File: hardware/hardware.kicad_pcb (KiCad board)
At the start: 2 copper layers, 1 part, among them U1 CH32V003F4P6

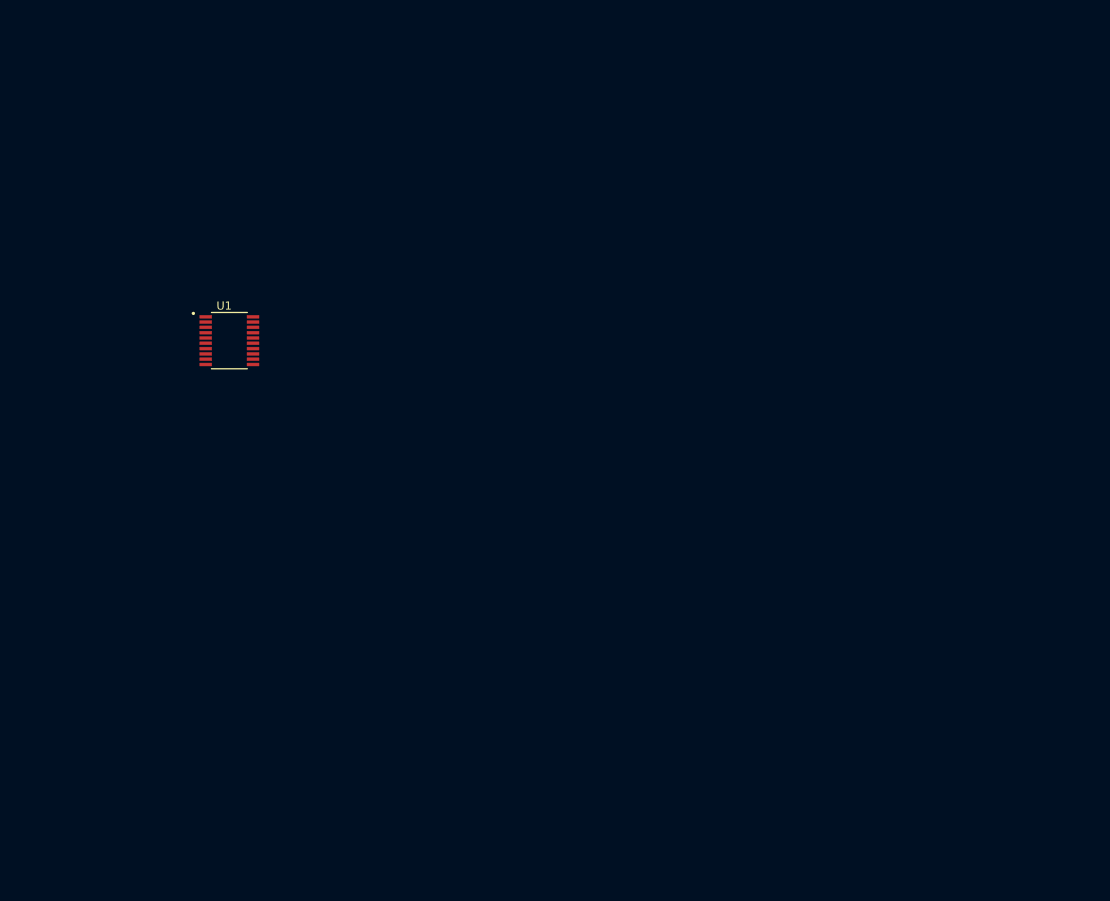
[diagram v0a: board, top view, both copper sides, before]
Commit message: add ch32v003 on pcb
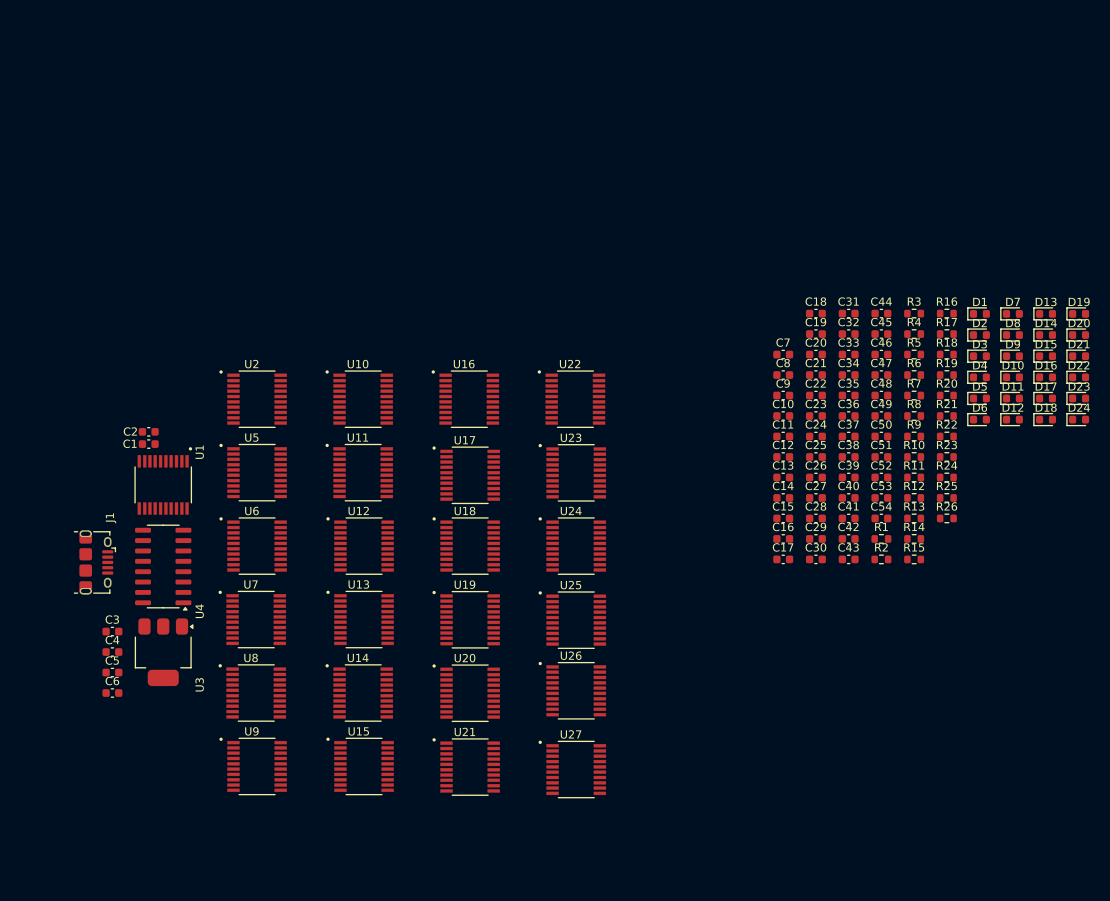
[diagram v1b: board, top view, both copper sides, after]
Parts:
- added C1: C_Small, Capacitor_SMD:C_0603_1608Metric, F.Cu at (49.7, 54.5)
- added C10: C_Small, Capacitor_SMD:C_0603_1608Metric, F.Cu at (127.5, 51.1)
- added C11: C_Small, Capacitor_SMD:C_0603_1608Metric, F.Cu at (127.5, 53.6)
- added C12: C_Small, Capacitor_SMD:C_0603_1608Metric, F.Cu at (127.5, 56.1)
- added C13: C_Small, Capacitor_SMD:C_0603_1608Metric, F.Cu at (127.5, 58.6)
- added C14: C_Small, Capacitor_SMD:C_0603_1608Metric, F.Cu at (127.5, 61.1)
- added C15: C_Small, Capacitor_SMD:C_0603_1608Metric, F.Cu at (127.5, 63.6)
- added C16: C_Small, Capacitor_SMD:C_0603_1608Metric, F.Cu at (127.5, 66.1)
- added C17: C_Small, Capacitor_SMD:C_0603_1608Metric, F.Cu at (127.5, 68.6)
- added C18: C_Small, Capacitor_SMD:C_0603_1608Metric, F.Cu at (131.5, 38.5)
- added C19: C_Small, Capacitor_SMD:C_0603_1608Metric, F.Cu at (131.5, 41.0)
- added C2: C_Small, Capacitor_SMD:C_0603_1608Metric, F.Cu at (49.7, 53.0)
- added C20: C_Small, Capacitor_SMD:C_0603_1608Metric, F.Cu at (131.5, 43.5)
- added C21: C_Small, Capacitor_SMD:C_0603_1608Metric, F.Cu at (131.5, 46.0)
- added C22: C_Small, Capacitor_SMD:C_0603_1608Metric, F.Cu at (131.5, 48.5)
- added C23: C_Small, Capacitor_SMD:C_0603_1608Metric, F.Cu at (131.5, 51.1)
- added C24: C_Small, Capacitor_SMD:C_0603_1608Metric, F.Cu at (131.5, 53.6)
- added C25: C_Small, Capacitor_SMD:C_0603_1608Metric, F.Cu at (131.5, 56.1)
- added C26: C_Small, Capacitor_SMD:C_0603_1608Metric, F.Cu at (131.5, 58.6)
- added C27: C_Small, Capacitor_SMD:C_0603_1608Metric, F.Cu at (131.5, 61.1)
- added C28: C_Small, Capacitor_SMD:C_0603_1608Metric, F.Cu at (131.5, 63.6)
- added C29: C_Small, Capacitor_SMD:C_0603_1608Metric, F.Cu at (131.5, 66.1)
- added C3: C, Capacitor_SMD:C_0603_1608Metric, F.Cu at (45.3, 77.5)
- added C30: C_Small, Capacitor_SMD:C_0603_1608Metric, F.Cu at (131.5, 68.6)
- added C31: C_Small, Capacitor_SMD:C_0603_1608Metric, F.Cu at (135.5, 38.5)
- added C32: C_Small, Capacitor_SMD:C_0603_1608Metric, F.Cu at (135.5, 41.0)
- added C33: C_Small, Capacitor_SMD:C_0603_1608Metric, F.Cu at (135.5, 43.5)
- added C34: C_Small, Capacitor_SMD:C_0603_1608Metric, F.Cu at (135.5, 46.0)
- added C35: C_Small, Capacitor_SMD:C_0603_1608Metric, F.Cu at (135.5, 48.5)
- added C36: C_Small, Capacitor_SMD:C_0603_1608Metric, F.Cu at (135.5, 51.1)
- added C37: C_Small, Capacitor_SMD:C_0603_1608Metric, F.Cu at (135.5, 53.6)
- added C38: C_Small, Capacitor_SMD:C_0603_1608Metric, F.Cu at (135.5, 56.1)
- added C39: C_Small, Capacitor_SMD:C_0603_1608Metric, F.Cu at (135.5, 58.6)
- added C4: C, Capacitor_SMD:C_0603_1608Metric, F.Cu at (45.3, 80.0)
- added C40: C_Small, Capacitor_SMD:C_0603_1608Metric, F.Cu at (135.5, 61.1)
- added C41: C_Small, Capacitor_SMD:C_0603_1608Metric, F.Cu at (135.5, 63.6)
- added C42: C_Small, Capacitor_SMD:C_0603_1608Metric, F.Cu at (135.5, 66.1)
- added C43: C_Small, Capacitor_SMD:C_0603_1608Metric, F.Cu at (135.5, 68.6)
- added C44: C_Small, Capacitor_SMD:C_0603_1608Metric, F.Cu at (139.5, 38.5)
- added C45: C_Small, Capacitor_SMD:C_0603_1608Metric, F.Cu at (139.5, 41.0)
- added C46: C_Small, Capacitor_SMD:C_0603_1608Metric, F.Cu at (139.5, 43.5)
- added C47: C_Small, Capacitor_SMD:C_0603_1608Metric, F.Cu at (139.5, 46.0)
- added C48: C_Small, Capacitor_SMD:C_0603_1608Metric, F.Cu at (139.5, 48.5)
- added C49: C_Small, Capacitor_SMD:C_0603_1608Metric, F.Cu at (139.5, 51.1)
- added C5: C, Capacitor_SMD:C_0603_1608Metric, F.Cu at (45.3, 82.5)
- added C50: C_Small, Capacitor_SMD:C_0603_1608Metric, F.Cu at (139.5, 53.6)
- added C51: C_Small, Capacitor_SMD:C_0603_1608Metric, F.Cu at (139.5, 56.1)
- added C52: C_Small, Capacitor_SMD:C_0603_1608Metric, F.Cu at (139.5, 58.6)
- added C53: C_Small, Capacitor_SMD:C_0603_1608Metric, F.Cu at (139.5, 61.1)
- added C54: C_Small, Capacitor_SMD:C_0603_1608Metric, F.Cu at (139.5, 63.6)
- added C6: C, Capacitor_SMD:C_0603_1608Metric, F.Cu at (45.3, 85.0)
- added C7: C_Small, Capacitor_SMD:C_0603_1608Metric, F.Cu at (127.5, 43.5)
- added C8: C_Small, Capacitor_SMD:C_0603_1608Metric, F.Cu at (127.5, 46.0)
- added C9: C_Small, Capacitor_SMD:C_0603_1608Metric, F.Cu at (127.5, 48.5)
- added D1: LED, LED_SMD:LED_0603_1608Metric, F.Cu at (151.6, 38.5)
- added D10: LED, LED_SMD:LED_0603_1608Metric, F.Cu at (155.6, 46.3)
- added D11: LED, LED_SMD:LED_0603_1608Metric, F.Cu at (155.6, 48.9)
- added D12: LED, LED_SMD:LED_0603_1608Metric, F.Cu at (155.6, 51.5)
- added D13: LED, LED_SMD:LED_0603_1608Metric, F.Cu at (159.7, 38.5)
- added D14: LED, LED_SMD:LED_0603_1608Metric, F.Cu at (159.7, 41.1)
- added D15: LED, LED_SMD:LED_0603_1608Metric, F.Cu at (159.7, 43.7)
- added D16: LED, LED_SMD:LED_0603_1608Metric, F.Cu at (159.7, 46.3)
- added D17: LED, LED_SMD:LED_0603_1608Metric, F.Cu at (159.7, 48.9)
- added D18: LED, LED_SMD:LED_0603_1608Metric, F.Cu at (159.7, 51.5)
- added D19: LED, LED_SMD:LED_0603_1608Metric, F.Cu at (163.7, 38.5)
- added D2: LED, LED_SMD:LED_0603_1608Metric, F.Cu at (151.6, 41.1)
- added D20: LED, LED_SMD:LED_0603_1608Metric, F.Cu at (163.7, 41.1)
- added D21: LED, LED_SMD:LED_0603_1608Metric, F.Cu at (163.7, 43.7)
- added D22: LED, LED_SMD:LED_0603_1608Metric, F.Cu at (163.7, 46.3)
- added D23: LED, LED_SMD:LED_0603_1608Metric, F.Cu at (163.7, 48.9)
- added D24: LED, LED_SMD:LED_0603_1608Metric, F.Cu at (163.7, 51.5)
- added D3: LED, LED_SMD:LED_0603_1608Metric, F.Cu at (151.6, 43.7)
- added D4: LED, LED_SMD:LED_0603_1608Metric, F.Cu at (151.6, 46.3)
- added D5: LED, LED_SMD:LED_0603_1608Metric, F.Cu at (151.6, 48.9)
- added D6: LED, LED_SMD:LED_0603_1608Metric, F.Cu at (151.6, 51.5)
- added D7: LED, LED_SMD:LED_0603_1608Metric, F.Cu at (155.6, 38.5)
- added D8: LED, LED_SMD:LED_0603_1608Metric, F.Cu at (155.6, 41.1)
- added D9: LED, LED_SMD:LED_0603_1608Metric, F.Cu at (155.6, 43.7)
- added J1: USB_B_Micro, Connector_USB:USB_Micro-B_Amphenol_10118194_Horizontal, F.Cu at (43.3, 69.0)
- added R1: R_Small, Resistor_SMD:R_0603_1608Metric, F.Cu at (139.5, 66.1)
- added R10: R_Small, Resistor_SMD:R_0603_1608Metric, F.Cu at (143.5, 56.1)
- added R11: R_Small, Resistor_SMD:R_0603_1608Metric, F.Cu at (143.5, 58.6)
- added R12: R_Small, Resistor_SMD:R_0603_1608Metric, F.Cu at (143.5, 61.1)
- added R13: R_Small, Resistor_SMD:R_0603_1608Metric, F.Cu at (143.5, 63.6)
- added R14: R_Small, Resistor_SMD:R_0603_1608Metric, F.Cu at (143.5, 66.1)
- added R15: R_Small, Resistor_SMD:R_0603_1608Metric, F.Cu at (143.5, 68.6)
- added R16: R_Small, Resistor_SMD:R_0603_1608Metric, F.Cu at (147.5, 38.5)
- added R17: R_Small, Resistor_SMD:R_0603_1608Metric, F.Cu at (147.5, 41.0)
- added R18: R_Small, Resistor_SMD:R_0603_1608Metric, F.Cu at (147.5, 43.5)
- added R19: R_Small, Resistor_SMD:R_0603_1608Metric, F.Cu at (147.5, 46.0)
- added R2: R_Small, Resistor_SMD:R_0603_1608Metric, F.Cu at (139.5, 68.6)
- added R20: R_Small, Resistor_SMD:R_0603_1608Metric, F.Cu at (147.5, 48.5)
- added R21: R_Small, Resistor_SMD:R_0603_1608Metric, F.Cu at (147.5, 51.1)
- added R22: R_Small, Resistor_SMD:R_0603_1608Metric, F.Cu at (147.5, 53.6)
- added R23: R_Small, Resistor_SMD:R_0603_1608Metric, F.Cu at (147.5, 56.1)
- added R24: R_Small, Resistor_SMD:R_0603_1608Metric, F.Cu at (147.5, 58.6)
- added R25: R_Small, Resistor_SMD:R_0603_1608Metric, F.Cu at (147.5, 61.1)
- added R26: R_Small, Resistor_SMD:R_0603_1608Metric, F.Cu at (147.5, 63.6)
- added R3: R_Small, Resistor_SMD:R_0603_1608Metric, F.Cu at (143.5, 38.5)
- added R4: R_Small, Resistor_SMD:R_0603_1608Metric, F.Cu at (143.5, 41.0)
- added R5: R_Small, Resistor_SMD:R_0603_1608Metric, F.Cu at (143.5, 43.5)
- added R6: R_Small, Resistor_SMD:R_0603_1608Metric, F.Cu at (143.5, 46.0)
- added R7: R_Small, Resistor_SMD:R_0603_1608Metric, F.Cu at (143.5, 48.5)
- added R8: R_Small, Resistor_SMD:R_0603_1608Metric, F.Cu at (143.5, 51.1)
- added R9: R_Small, Resistor_SMD:R_0603_1608Metric, F.Cu at (143.5, 53.6)
- added U10: CH32V003F4P6, CH32V003F4P6:SOP65P640X121-20N, F.Cu at (76.0, 49.0)
- added U11: CH32V003F4P6, CH32V003F4P6:SOP65P640X121-20N, F.Cu at (76.0, 58.0)
- added U12: CH32V003F4P6, CH32V003F4P6:SOP65P640X121-20N, F.Cu at (76.1, 67.0)
- added U13: CH32V003F4P6, CH32V003F4P6:SOP65P640X121-20N, F.Cu at (76.1, 76.0)
- added U14: CH32V003F4P6, CH32V003F4P6:SOP65P640X121-20N, F.Cu at (76.0, 85.0)
- added U15: CH32V003F4P6, CH32V003F4P6:SOP65P640X121-20N, F.Cu at (76.1, 94.0)
- added U16: CH32V003F4P6, CH32V003F4P6:SOP65P640X121-20N, F.Cu at (89.0, 49.0)
- added U17: CH32V003F4P6, CH32V003F4P6:SOP65P640X121-20N, F.Cu at (89.1, 58.3)
- added U18: CH32V003F4P6, CH32V003F4P6:SOP65P640X121-20N, F.Cu at (89.1, 67.0)
- added U19: CH32V003F4P6, CH32V003F4P6:SOP65P640X121-20N, F.Cu at (89.1, 76.0)
- added U2: CH32V003F4P6, CH32V003F4P6:SOP65P640X121-20N, F.Cu at (63.0, 49.0)
- added U20: CH32V003F4P6, CH32V003F4P6:SOP65P640X121-20N, F.Cu at (89.1, 85.0)
- added U21: CH32V003F4P6, CH32V003F4P6:SOP65P640X121-20N, F.Cu at (89.1, 94.1)
- added U22: CH32V003F4P6, CH32V003F4P6:SOP65P640X121-20N, F.Cu at (102.0, 49.0)
- added U23: CH32V003F4P6, CH32V003F4P6:SOP65P640X121-20N, F.Cu at (102.1, 58.0)
- added U24: CH32V003F4P6, CH32V003F4P6:SOP65P640X121-20N, F.Cu at (102.1, 67.0)
- added U25: CH32V003F4P6, CH32V003F4P6:SOP65P640X121-20N, F.Cu at (102.1, 76.1)
- added U26: CH32V003F4P6, CH32V003F4P6:SOP65P640X121-20N, F.Cu at (102.1, 84.7)
- added U27: CH32V003F4P6, CH32V003F4P6:SOP65P640X121-20N, F.Cu at (102.1, 94.4)
- added U3: AMS1117-3.3, Package_TO_SOT_SMD:SOT-223-3_TabPin2, F.Cu at (51.5, 80.0)
- added U4: CH340C, Package_SO:SOIC-16_3.9x9.9mm_P1.27mm, F.Cu at (51.5, 69.5)
- added U5: CH32V003F4P6, CH32V003F4P6:SOP65P640X121-20N, F.Cu at (63.0, 58.0)
- added U6: CH32V003F4P6, CH32V003F4P6:SOP65P640X121-20N, F.Cu at (63.0, 67.0)
- added U7: CH32V003F4P6, CH32V003F4P6:SOP65P640X121-20N, F.Cu at (62.9, 76.0)
- added U8: CH32V003F4P6, CH32V003F4P6:SOP65P640X121-20N, F.Cu at (62.9, 85.0)
- added U9: CH32V003F4P6, CH32V003F4P6:SOP65P640X121-20N, F.Cu at (63.0, 94.0)
- moved U1 19.4 mm to (51.5, 59.5), turned to -90 degrees
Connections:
- U1 pad 11: unconnected-(U1-PC1/SDA/NSS-Pad11) -> SDA
- U1 pad 12: unconnected-(U1-PC2/SCL/URTS/T1BKIN-Pad12) -> SCL
- U1 pad 18: unconnected-(U1-PD1/SWIO/T1CH3N/AETR2-Pad18) -> DIO0
- U1 pad 2: unconnected-(U1-PD5/UTX/A5-Pad2) -> RX-PROG
- U1 pad 3: unconnected-(U1-PD6/URX/A6-Pad3) -> TX-PROG
- U1 pad 7: unconnected-(U1-VSS-Pad7) -> GND
- U1 pad 9: unconnected-(U1-VDD-Pad9) -> +3V3

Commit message: position capacitor + resistor + led with each ch32
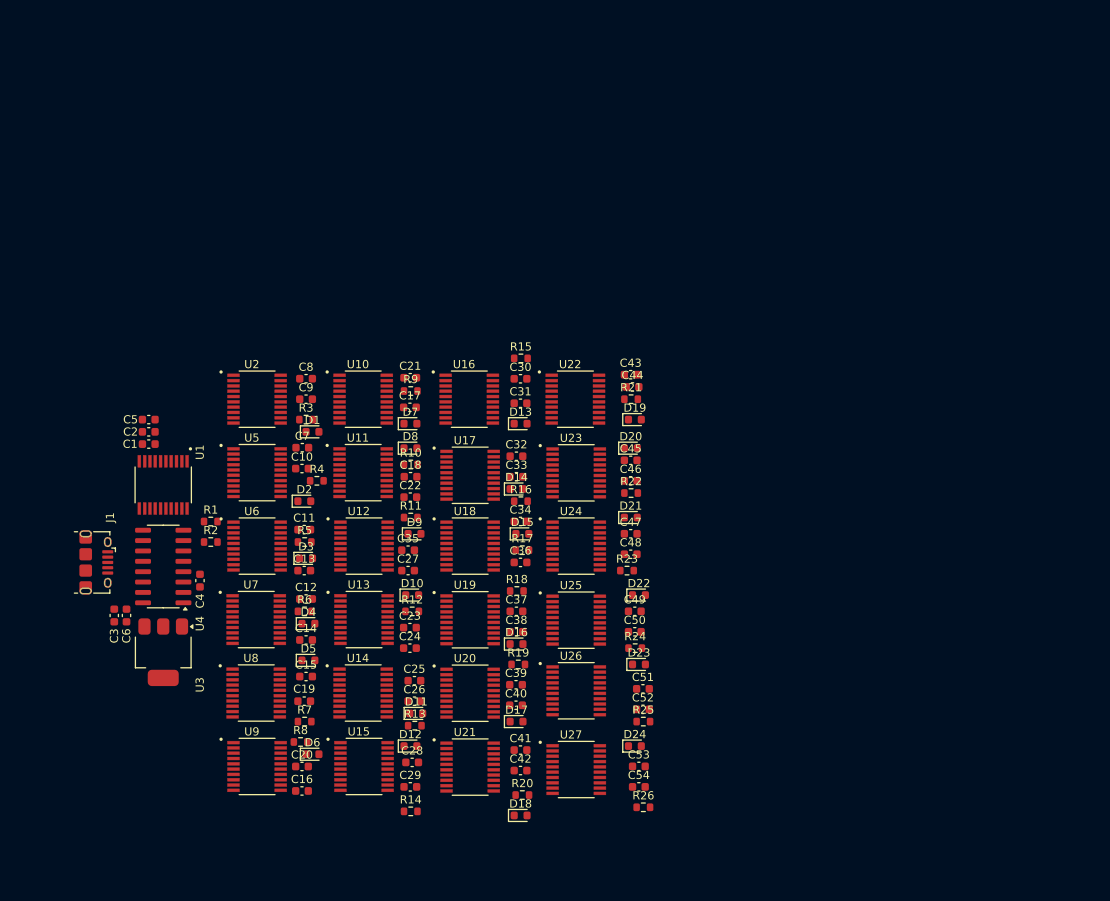
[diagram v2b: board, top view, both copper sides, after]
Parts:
- moved D6 91.5 mm to (69.8, 92.5)
- moved D5 88.3 mm to (69.3, 81.0)
- moved D4 87.6 mm to (69.3, 76.5)
- moved D3 86.2 mm to (69.0, 68.5)
- moved D2 85.2 mm to (68.8, 61.5)
- moved R8 85.1 mm to (68.3, 91.0)
- moved R7 84.7 mm to (68.8, 88.5)
- moved D12 84.0 mm to (81.8, 91.5)
- moved D1 83.0 mm to (69.8, 53.0)
- moved D11 82.7 mm to (82.5, 87.5)
- moved R1 82.2 mm to (57.3, 64.0)
- moved R2 82.2 mm to (57.3, 66.5)
- moved C20 80.7 mm to (68.5, 94.0)
- moved D18 80.6 mm to (95.3, 100.0)
- moved R6 80.1 mm to (68.8, 75.0)
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
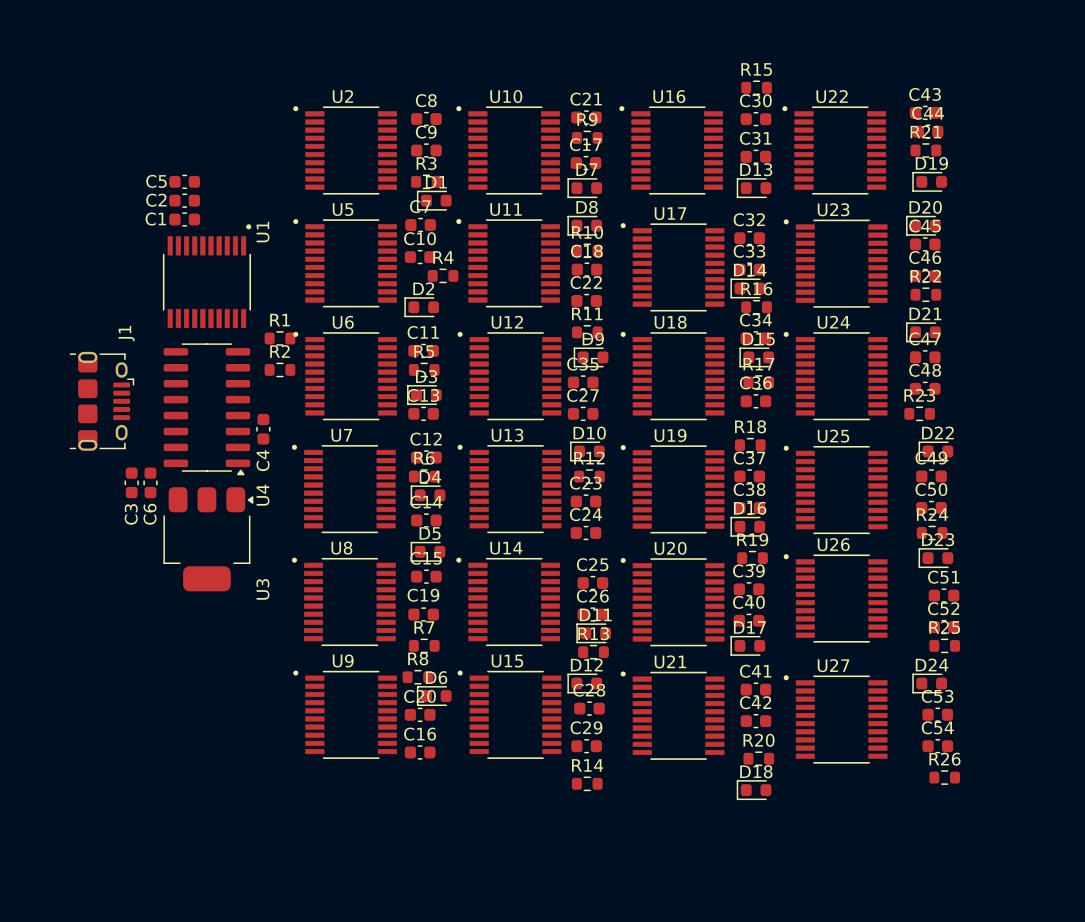
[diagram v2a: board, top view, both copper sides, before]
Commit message: add wiring ch32v006
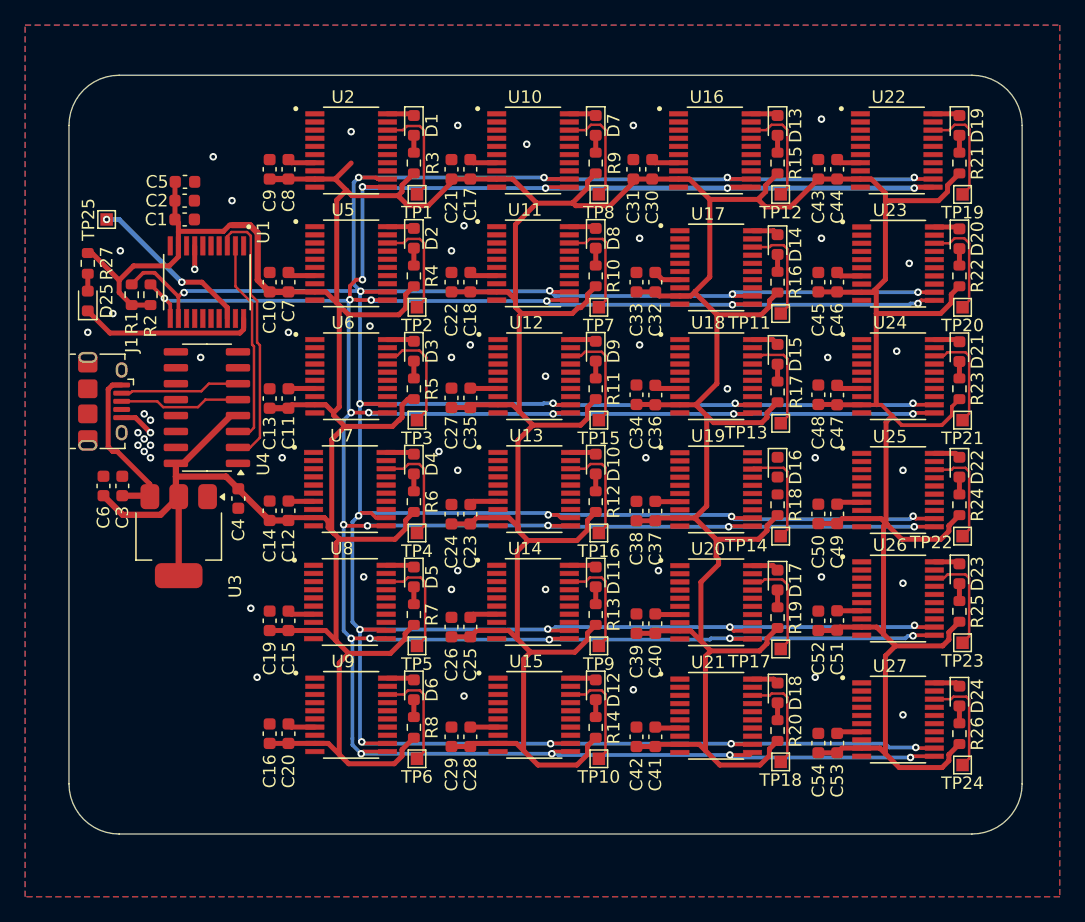
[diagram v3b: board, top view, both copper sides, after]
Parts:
- added D25: LED, LED_SMD:LED_0603_1608Metric, F.Cu at (42.0, 61.0)
- added R27: R_Small, Resistor_SMD:R_0603_1608Metric, F.Cu at (42.0, 58.0)
- added TP1: TestPoint, TestPoint:TestPoint_Pad_1.0x1.0mm, F.Cu at (68.2, 52.5)
- added TP10: TestPoint, TestPoint:TestPoint_Pad_1.0x1.0mm, F.Cu at (82.8, 97.5)
- added TP11: TestPoint, TestPoint:TestPoint_Pad_1.0x1.0mm, F.Cu at (97.2, 62.0)
- added TP12: TestPoint, TestPoint:TestPoint_Pad_1.0x1.0mm, F.Cu at (97.2, 52.5)
- added TP13: TestPoint, TestPoint:TestPoint_Pad_1.0x1.0mm, F.Cu at (97.2, 70.8)
- added TP14: TestPoint, TestPoint:TestPoint_Pad_1.0x1.0mm, F.Cu at (97.2, 79.8)
- added TP15: TestPoint, TestPoint:TestPoint_Pad_1.0x1.0mm, F.Cu at (82.8, 70.5)
- added TP16: TestPoint, TestPoint:TestPoint_Pad_1.0x1.0mm, F.Cu at (82.8, 79.5)
- added TP17: TestPoint, TestPoint:TestPoint_Pad_1.0x1.0mm, F.Cu at (97.2, 88.8)
- added TP18: TestPoint, TestPoint:TestPoint_Pad_1.0x1.0mm, F.Cu at (97.2, 97.8)
- added TP19: TestPoint, TestPoint:TestPoint_Pad_1.0x1.0mm, F.Cu at (111.8, 52.5)
- added TP2: TestPoint, TestPoint:TestPoint_Pad_1.0x1.0mm, F.Cu at (68.2, 61.5)
- added TP20: TestPoint, TestPoint:TestPoint_Pad_1.0x1.0mm, F.Cu at (111.8, 61.5)
- added TP21: TestPoint, TestPoint:TestPoint_Pad_1.0x1.0mm, F.Cu at (111.8, 70.5)
- added TP22: TestPoint, TestPoint:TestPoint_Pad_1.0x1.0mm, F.Cu at (111.8, 79.8)
- added TP23: TestPoint, TestPoint:TestPoint_Pad_1.0x1.0mm, F.Cu at (111.8, 88.2)
- added TP24: TestPoint, TestPoint:TestPoint_Pad_1.0x1.0mm, F.Cu at (111.8, 98.0)
- added TP25: TestPoint, TestPoint:TestPoint_Pad_1.0x1.0mm, F.Cu at (43.5, 54.5)
- added TP3: TestPoint, TestPoint:TestPoint_Pad_1.0x1.0mm, F.Cu at (68.2, 70.5)
- added TP4: TestPoint, TestPoint:TestPoint_Pad_1.0x1.0mm, F.Cu at (68.2, 79.5)
- added TP5: TestPoint, TestPoint:TestPoint_Pad_1.0x1.0mm, F.Cu at (68.2, 88.5)
- added TP6: TestPoint, TestPoint:TestPoint_Pad_1.0x1.0mm, F.Cu at (68.2, 97.5)
- added TP7: TestPoint, TestPoint:TestPoint_Pad_1.0x1.0mm, F.Cu at (82.8, 61.5)
- added TP8: TestPoint, TestPoint:TestPoint_Pad_1.0x1.0mm, F.Cu at (82.8, 52.5)
- added TP9: TestPoint, TestPoint:TestPoint_Pad_1.0x1.0mm, F.Cu at (82.8, 88.5)
- moved C9 12.6 mm to (56.5, 50.5), turned to 90 degrees
- moved C14 12.5 mm to (56.5, 77.7), turned to 90 degrees
- moved C13 12.3 mm to (56.5, 68.8), turned to 90 degrees
- moved R1 12.3 mm to (45.5, 60.5), turned to 90 degrees
- moved C19 12.3 mm to (56.5, 86.5), turned to 90 degrees
- moved C10 12.2 mm to (56.5, 59.5), turned to 90 degrees
- moved C16 12.1 mm to (56.5, 95.5), turned to 90 degrees
- moved R2 11.9 mm to (47.0, 60.5), turned to 90 degrees
- moved C12 11.8 mm to (58.0, 77.7), turned to 90 degrees
- moved C8 11.7 mm to (58.0, 50.5), turned to 90 degrees
- moved C15 11.5 mm to (58.0, 86.5), turned to 90 degrees
- moved C21 11.5 mm to (71.0, 50.5), turned to 90 degrees
- moved C7 11.5 mm to (58.0, 59.5), turned to 90 degrees
- moved C11 11.4 mm to (58.0, 68.8), turned to 90 degrees
- moved C26 11.3 mm to (71.0, 87.0), turned to 90 degrees
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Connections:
- U1 pad 18: DIO0 -> Net-(U1-PD1/SWIO/T1CH3N/AETR2)
- U1 pad 20: unconnected-(U1-PD3/A4/T2CH2/AETR/UCTS-Pad20) -> Net-(D25-K)
- U10 pad 18: DIO1 -> Net-(U10-PD1/SWIO/T1CH3N/AETR2)
- U11 pad 18: DIO1 -> Net-(U11-PD1/SWIO/T1CH3N/AETR2)
- U12 pad 18: DIO1 -> Net-(U12-PD1/SWIO/T1CH3N/AETR2)
- U13 pad 18: DIO1 -> Net-(U13-PD1/SWIO/T1CH3N/AETR2)
- U14 pad 18: DIO1 -> Net-(U14-PD1/SWIO/T1CH3N/AETR2)
- U15 pad 18: DIO1 -> Net-(U15-PD1/SWIO/T1CH3N/AETR2)
- U16 pad 18: DIO1 -> Net-(U16-PD1/SWIO/T1CH3N/AETR2)
- U17 pad 18: DIO1 -> Net-(U17-PD1/SWIO/T1CH3N/AETR2)
- U18 pad 18: DIO1 -> Net-(U18-PD1/SWIO/T1CH3N/AETR2)
- U19 pad 18: DIO1 -> Net-(U19-PD1/SWIO/T1CH3N/AETR2)
- U2 pad 18: DIO1 -> Net-(U2-PD1/SWIO/T1CH3N/AETR2)
- U20 pad 18: DIO1 -> Net-(U20-PD1/SWIO/T1CH3N/AETR2)
- U21 pad 18: DIO1 -> Net-(U21-PD1/SWIO/T1CH3N/AETR2)
- U22 pad 18: DIO1 -> Net-(U22-PD1/SWIO/T1CH3N/AETR2)
- U23 pad 18: DIO1 -> Net-(U23-PD1/SWIO/T1CH3N/AETR2)
- U24 pad 18: DIO1 -> Net-(U24-PD1/SWIO/T1CH3N/AETR2)
- U25 pad 18: DIO1 -> Net-(U25-PD1/SWIO/T1CH3N/AETR2)
- U26 pad 18: DIO1 -> Net-(U26-PD1/SWIO/T1CH3N/AETR2)
- U27 pad 18: DIO1 -> Net-(U27-PD1/SWIO/T1CH3N/AETR2)
- U5 pad 18: DIO1 -> Net-(U5-PD1/SWIO/T1CH3N/AETR2)
- U6 pad 18: DIO1 -> Net-(U6-PD1/SWIO/T1CH3N/AETR2)
- U7 pad 18: DIO1 -> Net-(U7-PD1/SWIO/T1CH3N/AETR2)
- U8 pad 18: DIO1 -> Net-(U8-PD1/SWIO/T1CH3N/AETR2)
- U9 pad 18: DIO1 -> Net-(U9-PD1/SWIO/T1CH3N/AETR2)
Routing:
- net +3V3: track 0.00 -> 572.7 mm
- net SCL: track 0.00 -> 378.0 mm, vias 0 -> 25
- net SDA: track 0.00 -> 374.6 mm, vias 0 -> 30
- net GND: track 0.00 -> 55.4 mm, vias 0 -> 54
- net TX-PROG: track 0.00 -> 21.4 mm
- net RX-PROG: track 0.00 -> 16.5 mm
- net Net-(D25-K): track 0.00 -> 14.1 mm
- net +5V: track 0.00 -> 13.6 mm
- net Net-(U1-PD1/SWIO/T1CH3N/AETR2): track 0.00 -> 13.4 mm, vias 0 -> 2
- net D+: track 0.00 -> 9.73 mm
- net D-: track 0.00 -> 9.59 mm
- net Net-(U6-PD1/SWIO/T1CH3N/AETR2): track 0.00 -> 8.82 mm
- net Net-(U8-PD1/SWIO/T1CH3N/AETR2): track 0.00 -> 8.76 mm
- net Net-(U7-PD1/SWIO/T1CH3N/AETR2): track 0.00 -> 8.67 mm
- net Net-(U22-PD1/SWIO/T1CH3N/AETR2): track 0.00 -> 8.65 mm
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- added copper zone on B.Cu, net GND
- added copper zone on F.Cu, net GND
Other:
- board outline added: 76 x 60.5 mm
